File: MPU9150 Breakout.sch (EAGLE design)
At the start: 22 parts, among them J401 M12PTH, U101 BMP180, U401 7432, U501 L3G4200D, U601 ADXL345, U801 5883

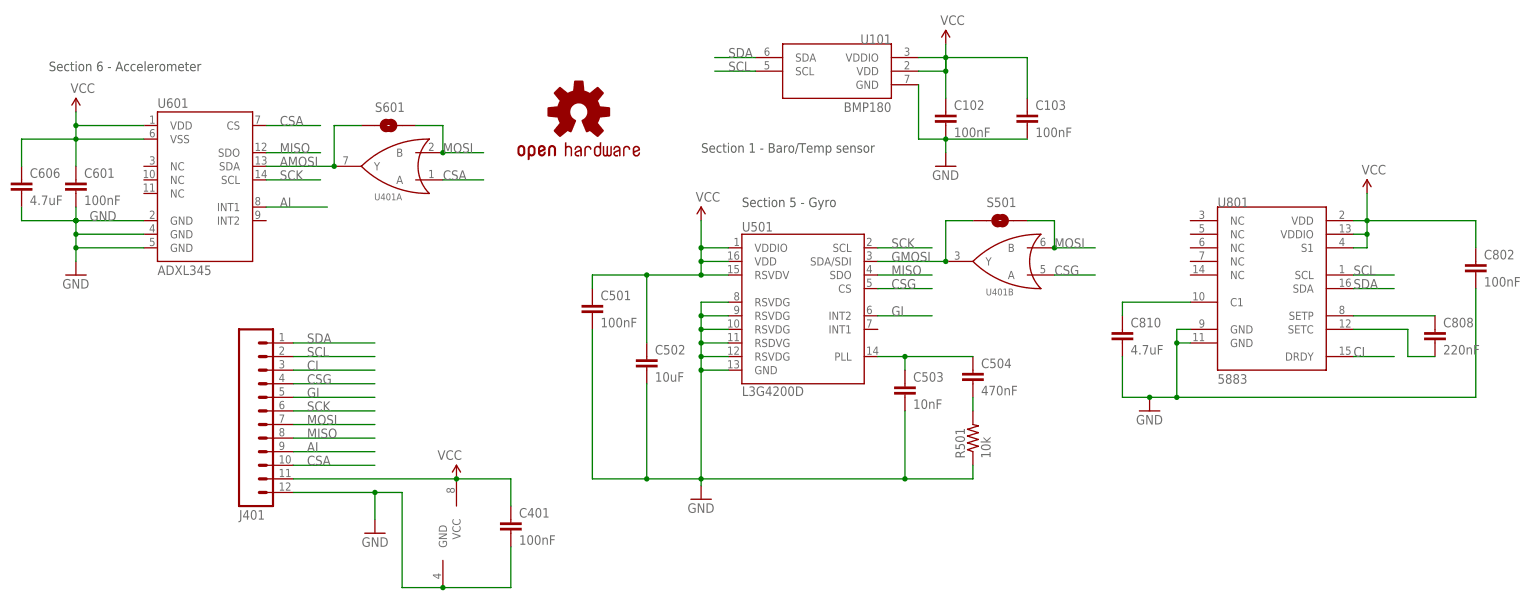
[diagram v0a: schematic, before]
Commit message: Merged Mio's KwanSystems.lbr, updated all eagle files to use it.
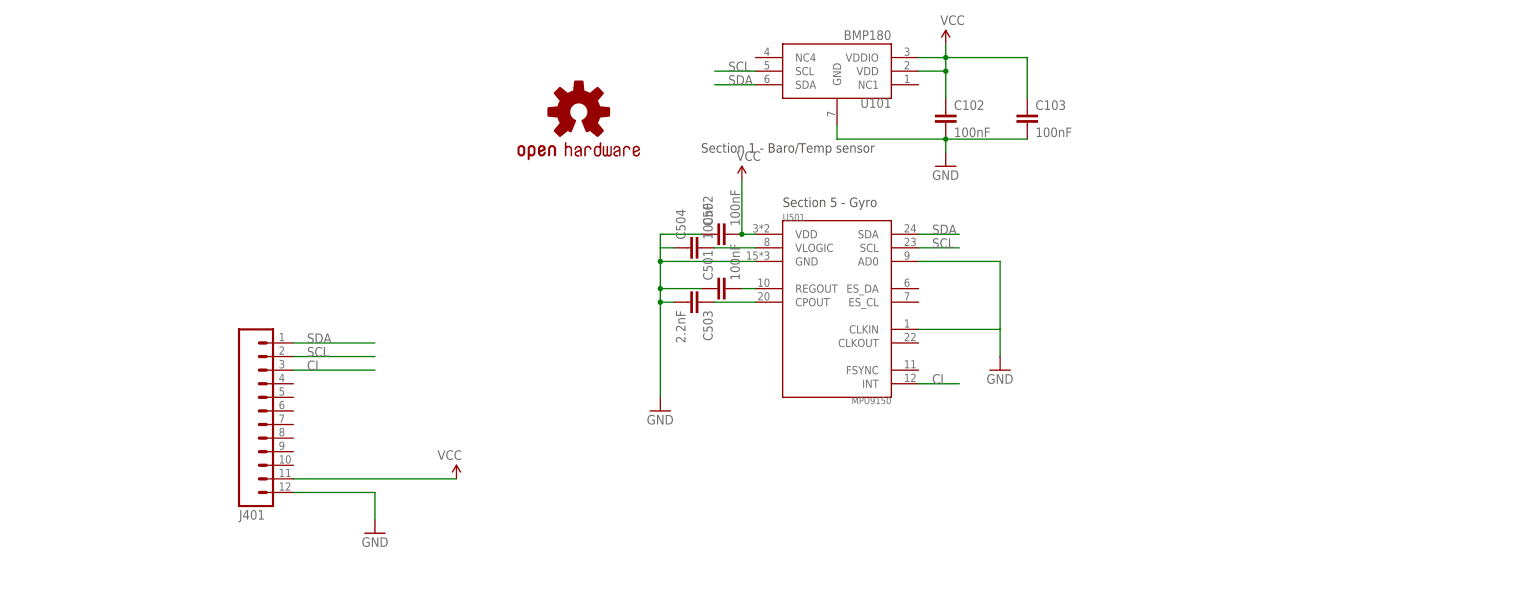
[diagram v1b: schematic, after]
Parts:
- removed C401, C601, C802: 100nF, SparkFun:CAP0603-CAP
- removed C606, C810: 4.7uF, SparkFun:CAP0603-CAP
- removed C808: 220nF, SparkFun:CAP0603-CAP
- removed R501: 10k, SparkFun:RESISTOR0603-RES
- removed S501, S601: SOLDERJUMPERNO, SparkFun:SOLDERJUMPERNO
- removed U401: 7432, KwanSystems:SN74LVC2G32
- removed U601: ADXL345, SparkFun:ADXL345
- removed U801: 5883, SparkFun:HMC5883LSMD
- C502: value 10uF -> 100nF; DIGIKEY 445-7486-1-ND -> 445-1316-1-ND
- C503: value 10nF -> 2.2nF; DIGIKEY 445-1311-1-ND -> 445-5132-1-ND
- C504: value 470nF -> 100nF; DIGIKEY 445-5192-1-ND -> 445-1316-1-ND
- U501: value L3G4200D -> MPU9150; device SparkFun:L3G4200D -> KwanSystems:MPU9150; DIGIKEY 497-11071-1-ND -> (none)
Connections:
- removed net AI: J401.9, U601.INT1
- removed net AMOSI: S601.1, U401A.Y, U601.SDA
- removed net CSA: J401.10, U401A.A, U601.CS
- removed net CSG: J401.4, U401B.A, U501.CS
- removed net GI: J401.5, U501.INT2
- removed net GMOSI: S501.1, U401B.Y, U501.SDA/SDI
- removed net MISO: J401.8, U501.SDO, U601.SDO
- removed net MOSI: J401.7, S501.2, S601.2, U401A.B, U401B.B
- removed net N$1: C503.1, C504.1, U501.PLL
- removed net N$14: C808.1, U801.SETP
- removed net N$15: C808.2, U801.SETC
- removed net N$16: C810.1, U801.C1
- removed net N$2: C504.2, R501.2
- removed net SCK: J401.6, U501.SCL, U601.SCL
- new net N$3: C503.1, U501.CPOUT
- new net N$5: C501.2, U501.REGOUT
- new net N$7: C504.2, U501.VLOGIC
- net CI: now also U501.INT; no longer U801.DRDY
- net GND: now also C501.1, C502.1, C504.1, U501.AD0, U501.CLKIN; no longer C401.2, C501.2, C502.2, C601.2, C606.2, C802.2, C810.2, R501.1, U401PWR.GND, U501.RSDVG@3, U501.RSVDG@0, U501.RSVDG@1, U501.RSVDG@2, U501.RSVDG@4, U601.GND@2, U601.GND@4, U601.GND@5, U801.GND@1, U801.GND@2
- net SCL: now also U501.SCL; no longer U801.SCL
- net SDA: now also U501.SDA; no longer U801.SDA
- net VCC: now also C502.2; no longer C401.1, C501.1, C502.1, C601.1, C606.1, C802.1, U401PWR.VCC, U501.RSVDV@0, U501.VDDIO, U601.VDD, U601.VSS, U801.S1, U801.VDD, U801.VDDIO
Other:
- note removed: "Section 6 - Accelerometer"
- moved on the sheet: C501, C502, C503, C504
